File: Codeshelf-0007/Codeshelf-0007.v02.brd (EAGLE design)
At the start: 103.5 x 53 mm, 28 parts, among them J1 RJ45-8PTH, J2 RJ45-8PTH, U2 MC9S08QG-DT, U3 CAT9552, U4 RS485SOIC, U7 7SEGMENT-2DIGIT

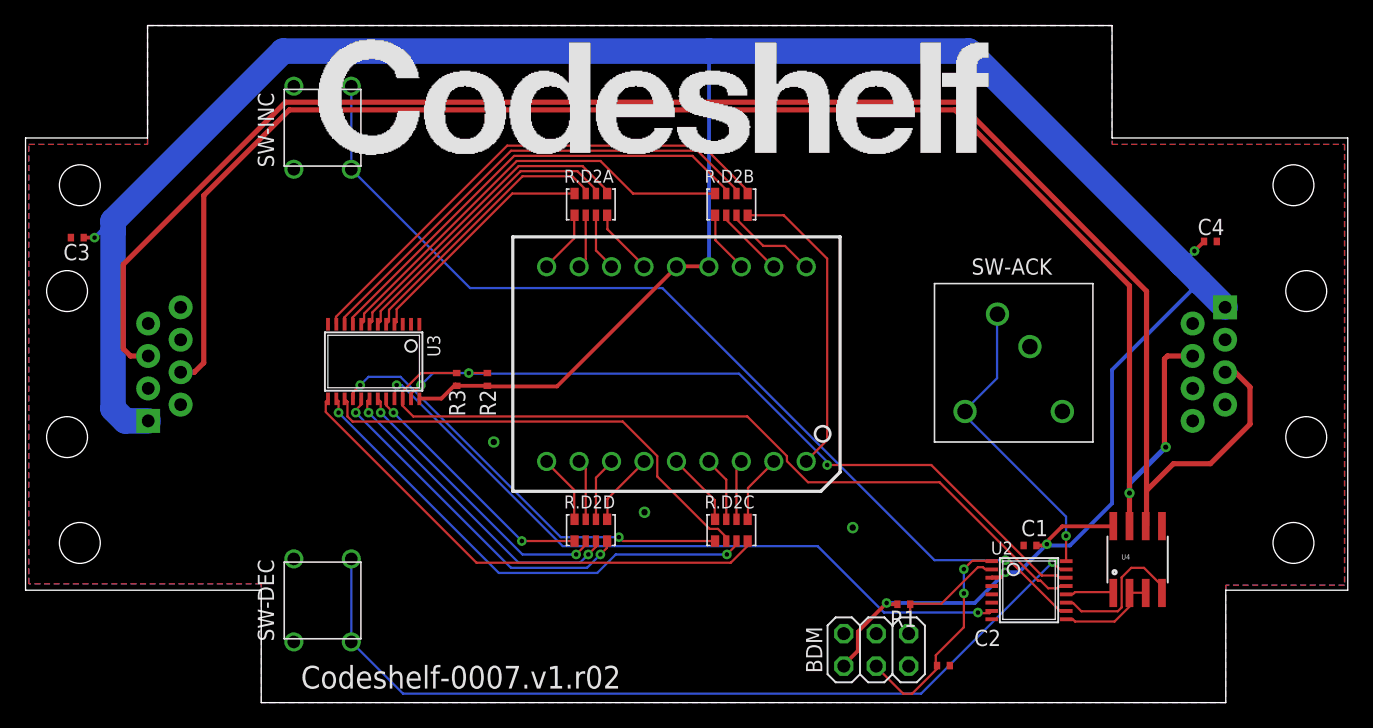
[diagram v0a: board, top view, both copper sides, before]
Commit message: Changes related to design review with Ravi and Charlie.
Mainly we need a new way to connect all of the boards where the cables
enter the back.
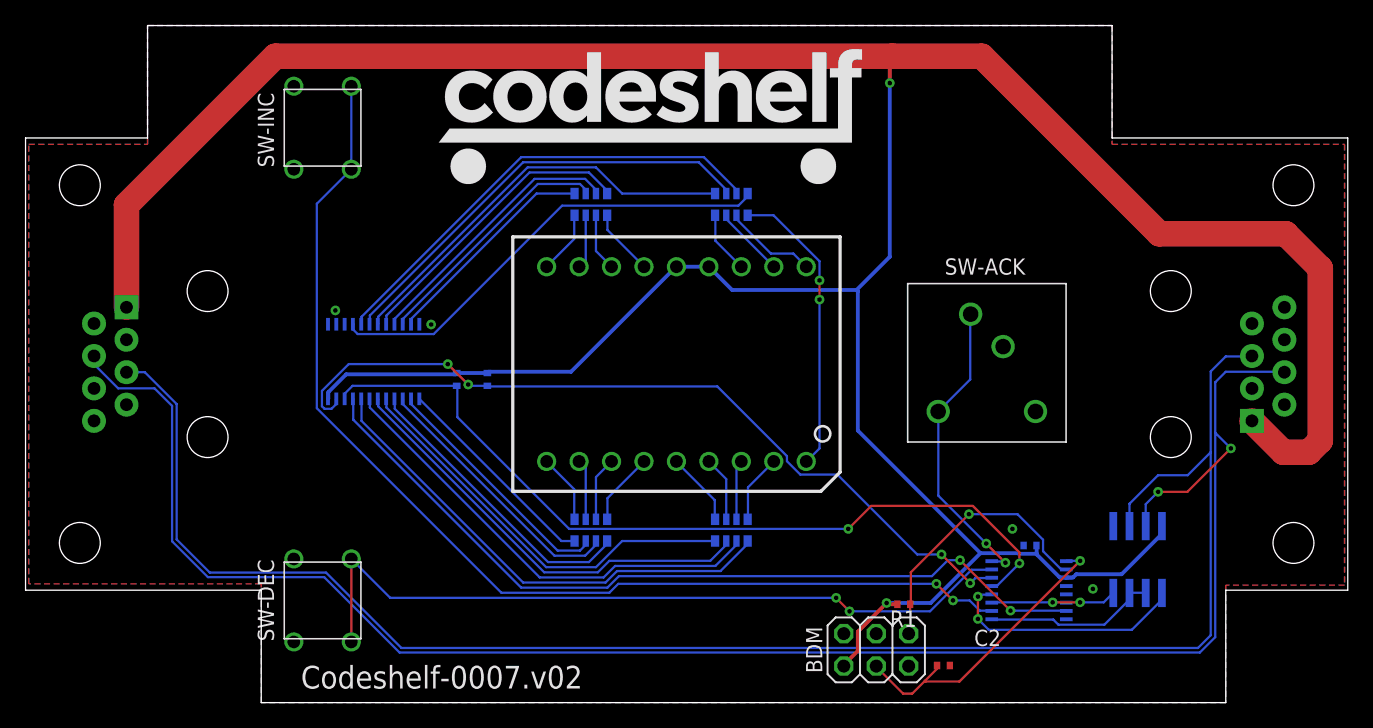
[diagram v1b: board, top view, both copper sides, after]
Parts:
- removed C3, C4: .1uF, GW-devices:C0402
- moved ACK.BUTTON.KEYCAP 115.3 mm to (95.7, 50.9)
- moved STANDOFF2 115.3 mm to (92.5, 47.5)
- moved STANDOFF3 115.3 mm to (91.5, 46.4)
- moved CASE 115.3 mm to (97.3, 52.6)
- moved STANDOFF1 115.3 mm to (94.1, 49.2)
- moved STANDOFF4 114.8 mm to (88.7, 47.7)
- moved LOGO 16.1 mm to (32.1, 40.6)
- moved J2 11.0 mm to (14.0, 26.5), turned to 270 degrees
- moved J1 10.6 mm to (89.4, 26.5), turned to 90 degrees
- moved SW-ACK 2.10 mm to (75.0, 26.6)
- flipped C1 to the bottom, turned to 0 degrees
- flipped R.D2A to the bottom
- flipped R.D2B to the bottom
- flipped R.D2C to the bottom
- flipped R.D2D to the bottom
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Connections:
- net A renamed RS485_P
- net B renamed RS485_N
- removed net N$39: R.D2C.3, U3.14
- removed net N$40: R.D2C.4, U3.13
- new net N$1: R.D2A.5, U3.11
- new net N$21: R.D2A.4, U7.18
- net +3V3: no longer C3.1, C4.1
- net GND: no longer C3.2, C4.2
- net N$10: now also R.D2B.6, U3.6; no longer R.D2B.1, U7.12
- net N$11: now also R.D2B.7, U3.5; no longer R.D2B.2, U7.11
- net N$12: now also R.D2B.8, U3.4; no longer R.D2B.3, U7.10
- net N$13: now also U7.4; no longer U7.1
- net N$14: now also U7.3; no longer U7.2
- net N$15: now also U7.2; no longer U7.3
- net N$16: now also U7.1; no longer U7.4
- net N$17: now also R.D2A.1, U7.15; no longer R.D2C.8, U7.5
- net N$18: now also R.D2A.2, U7.16; no longer R.D2C.7, U7.6
- net N$2: now also R.D2A.6, U3.10; no longer R.D2A.1, U7.18
- net N$20: now also R.D2A.3, U7.17; no longer R.D2C.6, U7.7
- net N$22: now also R.D2B.4, U7.12; no longer R.D2C.5, U7.8
- net N$24: now also R.D2B.3, U7.11; no longer R.D2B.4, U7.9
- net N$25: now also R.D2C.8, U7.8; no longer R.D2A.8, U3.4
- net N$26: now also R.D2C.7, U7.7; no longer R.D2A.7, U3.5
- net N$27: now also R.D2C.6, U7.6; no longer R.D2A.6, U3.6
- net N$28: now also R.D2C.5, U7.5; no longer R.D2A.5, U3.7
- net N$29: now also R.D2B.1, U7.9; no longer R.D2B.8, U3.8
- net N$3: now also R.D2A.7, U3.9; no longer R.D2A.2, U7.17
- net N$30: now also R.D2B.2, U7.10; no longer R.D2B.7, U3.9
- net N$31: now also R.D2D.4, U3.13; no longer R.D2B.6, U3.10
- net N$32: now also R.D2D.3, U3.14; no longer R.D2B.5, U3.11
- net N$33: now also R.D2D.2, U3.15; no longer R.D2D.1, U3.20
- net N$34: now also R.D2D.1, U3.16; no longer R.D2D.2, U3.19
- net N$35: now also R.D2C.4, U3.17; no longer R.D2D.3, U3.18
- net N$36: now also R.D2C.3, U3.18; no longer R.D2D.4, U3.17
- net N$37: now also R.D2C.2, U3.19; no longer R.D2C.1, U3.16
- net N$38: now also R.D2C.1, U3.20; no longer R.D2C.2, U3.15
- net N$4: now also R.D2A.8, U3.8; no longer R.D2A.3, U7.16
- net N$5: now also R.D2B.5, U3.7; no longer R.D2A.4, U7.15
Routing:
- net N$40: track 40.0 -> 0.00 mm
- net N$39: track 38.7 -> 0.00 mm, vias 2 -> 0
- net +3V3: track 224.1 -> 258.1 mm, vias 5 -> 2
- net N$11: track 5.61 -> 36.5 mm
- net N$10: track 4.91 -> 34.8 mm
- net N$30: track 36.4 -> 7.31 mm
- net N$12: track 7.33 -> 36.2 mm
- net N$5: track 5.28 -> 32.7 mm
- net N$31: track 38.2 -> 16.8 mm
- net N$32: track 40.1 -> 19.3 mm
- net N$28: track 25.2 -> 5.80 mm
- net N$4: track 4.56 -> 23.4 mm
- net N$24: track 24.2 -> 5.57 mm
- net N$27: track 23.4 -> 5.09 mm
- net N$1: track 0.00 -> 17.3 mm
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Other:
- board text added: "Codeshelf-0007.v02"
- board text removed: "Codeshelf-0007.v1.r02"

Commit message: Position controller bus rewiring
The position controller's RS495 bus rewired to support double 3.3V/GND
and to be off of the same pins as the scanner.  (Matches the change
with the CHE controller.)
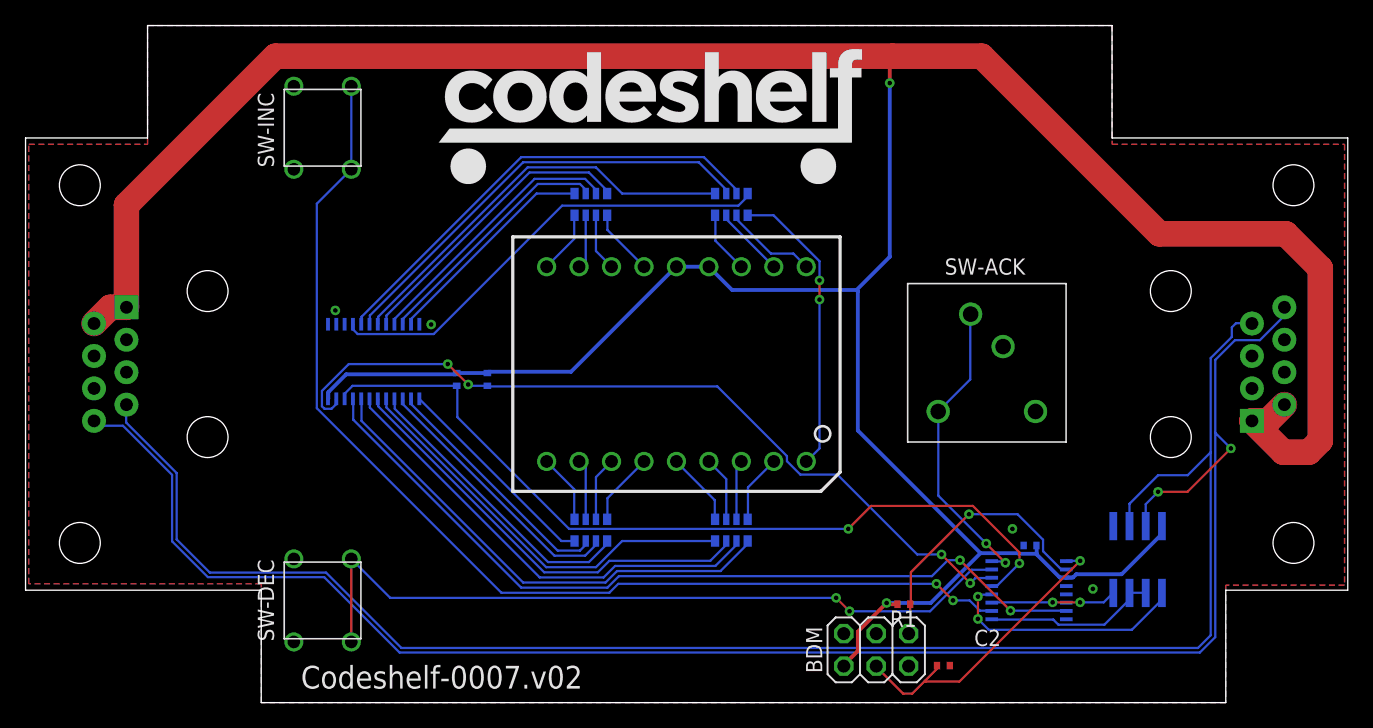
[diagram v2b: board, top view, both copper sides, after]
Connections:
- net +3V3: now also J1.2, J2.2
- net GND: now also J1.3, J1.6, J2.3, J2.6; no longer J1.8, J2.8
- net RS485_N: now also J1.8, J2.8; no longer J1.4, J2.4
- net RS485_P: now also J1.7, J2.7; no longer J1.5, J2.5
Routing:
- net +3V3: track 258.1 -> 264.2 mm
- net RS485_N: track 142.1 -> 140.0 mm
- net RS485_P: track 134.6 -> 133.4 mm
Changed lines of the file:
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@@
 <contactref element="SW-DEC" pad="P$3"/>
 <contactref element="SW-ACK" pad="P$3"/>
-<contactref element="J1" pad="8"/>
-<contactref element="J2" pad="8"/>
 <polygon width="0.4064" layer="1">
 <vertex x="0" y="9.3"/>
@@
 <via x="77" y="13.6" extent="1-16" drill="0.3556"/>
 <via x="83.3" y="8.9" extent="1-16" drill="0.3556"/>
+<contactref element="J2" pad="6"/>
+<contactref element="J2" pad="3"/>
+<contactref element="J1" pad="3"/>
+<contactref element="J1" pad="6"/>
 </signal>
 <signal name="+3V3" class="1">
@@
 <wire x1="64.9" y1="32.2" x2="64.8" y2="32.3" width="0.3" layer="16"/>
 <via x="67.15" y="7.8" extent="1-16" drill="0.3556"/>
+<contactref element="J2" pad="2"/>
+<contactref element="J1" pad="2"/>
+<wire x1="7.65" y1="30.945" x2="6.38" y2="30.945" width="2" layer="1"/>
+<wire x1="6.38" y1="30.945" x2="5.11" y2="29.675" width="2" layer="1"/>
+<wire x1="95.75" y1="22.055" x2="97.02" y2="22.055" width="2" layer="1"/>
+<wire x1="97.02" y1="22.055" x2="98.29" y2="23.325" width="2" layer="1"/>
 </signal>
 <signal name="SLC">
@@
 </signal>
 <signal name="RS485_N">
-<contactref element="J2" pad="4"/>
-<contactref element="J1" pad="4"/>
 <contactref element="U4" pad="7"/>
-<wire x1="5.11" y1="27.135" x2="5.11" y2="26.49" width="0.1778" layer="16"/>
-<wire x1="5.11" y1="26.49" x2="7" y2="24.6" width="0.1778" layer="16"/>
-<wire x1="7" y1="24.6" x2="9.84855" y2="24.6" width="0.1778" layer="16"/>
-<wire x1="9.84855" y1="24.6" x2="11.2222" y2="23.22635" width="0.1778" layer="16"/>
-<wire x1="11.2222" y1="23.22635" x2="11.2222" y2="12.62635" width="0.1778" layer="16"/>
 <wire x1="11.2222" y1="12.62635" x2="14.02635" y2="9.8222" width="0.1778" layer="16"/>
 <wire x1="14.02635" y1="9.8222" x2="23.12635" y2="9.8222" width="0.1778" layer="16"/>
@@
 <wire x1="91.67365" y1="3.9222" x2="92.8778" y2="5.12635" width="0.1778" layer="16"/>
 <wire x1="92.8778" y1="5.12635" x2="92.8778" y2="21.1222" width="0.1778" layer="16"/>
-<wire x1="92.8778" y1="21.1222" x2="92.8778" y2="25.0778" width="0.1778" layer="16"/>
-<wire x1="92.8778" y1="25.0778" x2="93.7" y2="25.9" width="0.1778" layer="16"/>
-<wire x1="93.7" y1="25.9" x2="98.255" y2="25.9" width="0.1778" layer="16"/>
-<wire x1="98.255" y1="25.9" x2="98.29" y2="25.865" width="0.1778" layer="16"/>
 <wire x1="87.435" y1="13.8162" x2="87.435" y2="15.535" width="0.1778" layer="16"/>
 <wire x1="87.435" y1="15.535" x2="88.4" y2="16.5" width="0.1778" layer="16"/>
@@
 <via x="94.1" y="19.9" extent="1-16" drill="0.3556"/>
 <wire x1="94.1" y1="19.9" x2="92.8778" y2="21.1222" width="0.1778" layer="16"/>
+<wire x1="92.8778" y1="21.1222" x2="92.8778" y2="26.82635" width="0.1778" layer="16"/>
+<contactref element="J2" pad="8"/>
+<contactref element="J1" pad="8"/>
+<wire x1="11.2222" y1="12.62635" x2="11.2222" y2="17.82635" width="0.1778" layer="16"/>
+<wire x1="11.2222" y1="17.82635" x2="7.374275" y2="21.674275" width="0.1778" layer="16"/>
+<wire x1="7.374275" y1="21.674275" x2="5.490725" y2="21.674275" width="0.1778" layer="16"/>
+<wire x1="5.490725" y1="21.674275" x2="5.11" y2="22.055" width="0.1778" layer="16"/>
+<wire x1="92.8778" y1="26.82635" x2="94.425725" y2="28.374275" width="0.1778" layer="16"/>
+<wire x1="94.425725" y1="28.374275" x2="96.374275" y2="28.374275" width="0.1778" layer="16"/>
+<wire x1="96.374275" y1="28.374275" x2="98.3" y2="30.3" width="0.1778" layer="16"/>
+<wire x1="98.3" y1="30.3" x2="98.3" y2="30.935" width="0.1778" layer="16"/>
+<wire x1="98.3" y1="30.935" x2="98.29" y2="30.945" width="0.1778" layer="16"/>
 </signal>
 <signal name="N$6">
@@
 </signal>
 <signal name="RS485_P">
-<contactref element="J2" pad="5"/>
 <contactref element="U4" pad="6"/>
-<contactref element="J1" pad="5"/>
-<wire x1="7.65" y1="25.865" x2="9.08645" y2="25.865" width="0.1778" layer="16"/>
-<wire x1="9.08645" y1="25.865" x2="11.5778" y2="23.37365" width="0.1778" layer="16"/>
-<wire x1="11.5778" y1="23.37365" x2="11.5778" y2="12.77365" width="0.1778" layer="16"/>
 <wire x1="11.5778" y1="12.77365" x2="14.17365" y2="10.1778" width="0.1778" layer="16"/>
 <wire x1="14.17365" y1="10.1778" x2="23.27365" y2="10.1778" width="0.1778" layer="16"/>
@@
 <wire x1="91.52635" y1="4.2778" x2="92.5222" y2="5.27365" width="0.1778" layer="16"/>
 <wire x1="92.5222" y1="5.27365" x2="92.5222" y2="19.6" width="0.1778" layer="16"/>
-<wire x1="92.5222" y1="19.6" x2="92.5222" y2="25.9222" width="0.1778" layer="16"/>
-<wire x1="92.5222" y1="25.9222" x2="93.7" y2="27.1" width="0.1778" layer="16"/>
-<wire x1="93.7" y1="27.1" x2="95.715" y2="27.1" width="0.1778" layer="16"/>
-<wire x1="95.715" y1="27.1" x2="95.75" y2="27.135" width="0.1778" layer="16"/>
+<wire x1="92.5222" y1="19.6" x2="92.5222" y2="26.97365" width="0.1778" layer="16"/>
 <wire x1="86.165" y1="13.8162" x2="86.165" y2="15.565" width="0.1778" layer="16"/>
 <wire x1="86.165" y1="15.565" x2="88.4" y2="17.8" width="0.1778" layer="16"/>
 <wire x1="88.4" y1="17.8" x2="90.7222" y2="17.8" width="0.1778" layer="16"/>
 <wire x1="90.7222" y1="17.8" x2="92.5222" y2="19.6" width="0.1778" layer="16"/>
+<contactref element="J2" pad="7"/>
+<contactref element="J1" pad="7"/>
+<wire x1="11.5778" y1="12.77365" x2="11.5778" y2="17.97365" width="0.1778" layer="16"/>
+<wire x1="11.5778" y1="17.97365" x2="7.625725" y2="21.925725" width="0.1778" layer="16"/>
+<wire x1="7.625725" y1="21.925725" x2="7.625725" y2="23.300725" width="0.1778" layer="16"/>
+<wire x1="7.625725" y1="23.300725" x2="7.65" y2="23.325" width="0.1778" layer="16"/>
+<wire x1="92.5222" y1="26.97365" x2="94.174275" y2="28.625725" width="0.1778" layer="16"/>
+<wire x1="94.174275" y1="28.625725" x2="94.174275" y2="29.374275" width="0.1778" layer="16"/>
+<wire x1="94.174275" y1="29.374275" x2="94.5" y2="29.7" width="0.1778" layer="16"/>
+<wire x1="94.5" y1="29.7" x2="95.725" y2="29.7" width="0.1778" layer="16"/>
+<wire x1="95.725" y1="29.7" x2="95.75" y2="29.675" width="0.1778" layer="16"/>
 </signal>
 <signal name="N$1">

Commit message: Changes reviewed with Charlie
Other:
- board text added: "CS0007.2013.11.24.n1"
- board text removed: "Codeshelf-0007.v02"
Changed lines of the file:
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@@
 <wire x1="84.8" y1="53" x2="84.8" y2="44.2" width="0" layer="20"/>
 <wire x1="84.8" y1="44.2" x2="103.25" y2="44.2" width="0" layer="20"/>
-<text x="21.3" y="1.1" size="1.778" layer="21">Codeshelf-0007.v02</text>
+<text x="23.3" y="1.1" size="1.778" layer="21">CS0007.2013.11.24.n1</text>
 <hole x="4" y="12.5" drill="3.2"/>
 <hole x="4" y="40.5" drill="3.2"/>
@@
 <element name="LOGO" library="GW-devices" package="CODESHELF-LOGO" value="CODESHELF-LOGO" x="32.1" y="40.6"/>
 <element name="BDM" library="GW-devices" package="HEADER-3X2" value="HEADER-3X2" x="63.8" y="5.4" smashed="yes" rot="R180">
-<attribute name="NAME" x="60.845" y="5.95" size="1.27" layer="25" ratio="10" rot="R270"/>
+<attribute name="NAME" x="60.645" y="8.05" size="1.27" layer="25" ratio="10" rot="R270"/>
 </element>
 <element name="R1" library="GW-devices" package="RF-R0402" value="3.3K" x="68.5" y="7.7" smashed="yes" rot="R180">
@@
 </element>
 <element name="SW-DEC" library="GW-devices" package="SWITCH-TACTILE-FSM" value="SWITCH-TACTILE-FSM" x="23" y="8" smashed="yes" rot="R270">
-<attribute name="NAME" x="19.2" y="4.8" size="1.27" layer="25" rot="R90"/>
+<attribute name="NAME" x="26.8" y="13.6" size="1.27" layer="25" rot="R180"/>
 <attribute name="MFGN" value="TE Connectivity" x="23" y="8" size="1.778" layer="27" rot="R270" display="off"/>
 <attribute name="MFGP" value="FSM16JH" x="23" y="8" size="1.778" layer="27" rot="R270" display="off"/>
@@
 </element>
 <element name="SW-INC" library="GW-devices" package="SWITCH-TACTILE-FSM" value="SWITCH-TACTILE-FSM" x="23" y="45" smashed="yes" rot="R270">
-<attribute name="NAME" x="19.2" y="41.9" size="1.27" layer="25" rot="R90"/>
+<attribute name="NAME" x="19.9" y="39.4" size="1.27" layer="25"/>
 <attribute name="MFGN" value="TE Connectivity" x="23" y="45" size="1.778" layer="27" rot="R270" display="off"/>
 <attribute name="MFGP" value="FSM16JH" x="23" y="45" size="1.778" layer="27" rot="R270" display="off"/>

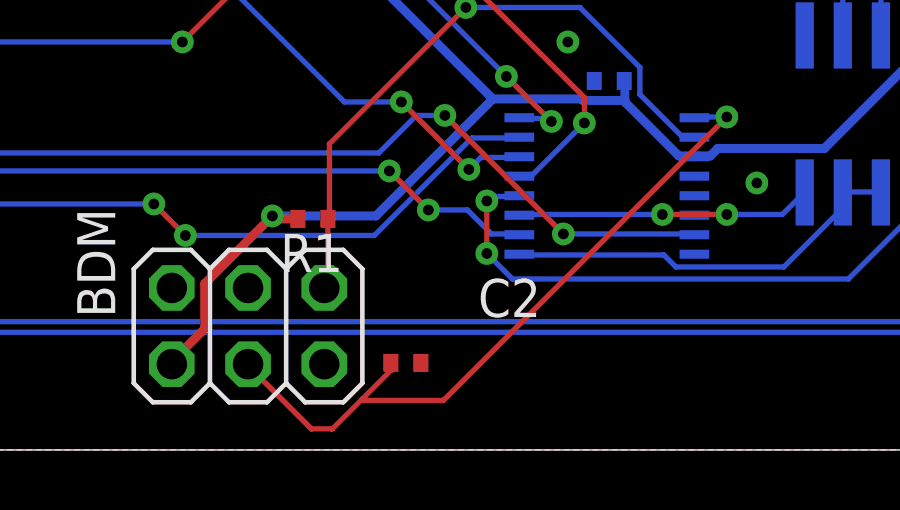
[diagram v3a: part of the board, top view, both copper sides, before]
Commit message: BOM review before first articles of 0005, 0007, 0008, 0012
Reviewed BOM with Charlie
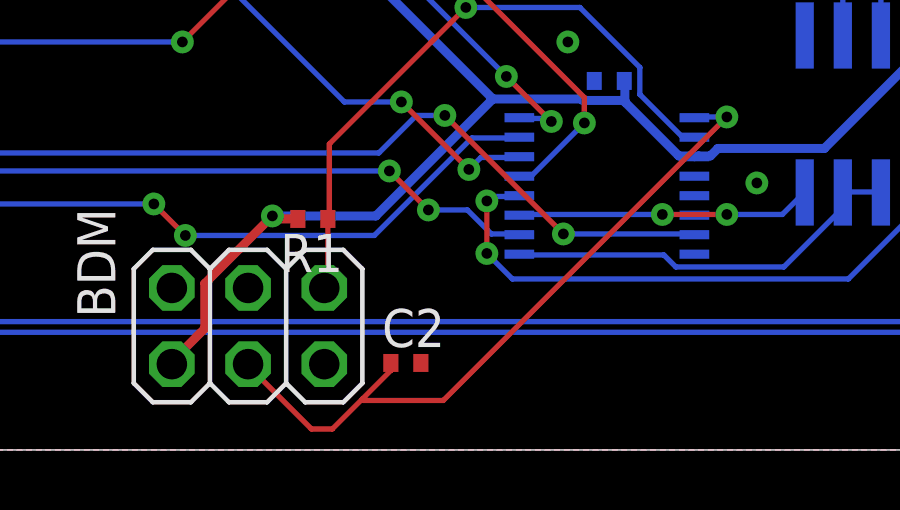
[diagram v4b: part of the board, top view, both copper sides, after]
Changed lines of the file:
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@@
 <attribute name="NAME" x="79.78" y="10.3" size="1.27" layer="26" rot="MR0"/>
 <attribute name="MFGN" value="Murata" x="78.38" y="12.3" size="1.778" layer="28" rot="MR0" display="off"/>
-<attribute name="MFGP" value="GRM033R61A104KE15D" x="78.38" y="12.3" size="1.778" layer="28" rot="MR0" display="off"/>
+<attribute name="MFGP" value="
+GRM155R61C104KA88D" x="78.38" y="12.3" size="1.778" layer="28" rot="MR0" display="off"/>
 <attribute name="PRICE" value="0.02" x="78.38" y="12.3" size="1.778" layer="28" rot="MR0" display="off"/>
 </element>
@@
 </element>
 <element name="C2" library="GW-devices" package="C0402" value=".1uF" x="71.6" y="2.9" smashed="yes" rot="R180">
-<attribute name="NAME" x="76.1" y="5.7" size="1.27" layer="25" rot="R180"/>
+<attribute name="NAME" x="72.9" y="4.7" size="1.27" layer="25" rot="R180"/>
 <attribute name="MFGN" value="Murata" x="71.6" y="2.9" size="1.778" layer="27" rot="R180" display="off"/>
-<attribute name="MFGP" value="GRM033R61A104KE15D" x="71.6" y="2.9" size="1.778" layer="27" rot="R180" display="off"/>
+<attribute name="MFGP" value="
+GRM155R61C104KA88D" x="71.6" y="2.9" size="1.778" layer="27" rot="R180" display="off"/>
 <attribute name="PRICE" value="0.02" x="71.6" y="2.9" size="1.778" layer="27" rot="R180" display="off"/>
 </element>
@@
 <attribute name="NAME" x="35.3" y="26.1" size="1.27" layer="26" rot="MR90"/>
 <attribute name="MFGN" value="Panasonic" x="35.9" y="25.3" size="1.778" layer="28" rot="MR90" display="off"/>
-<attribute name="MFGP" value="ERJ-2GEJ332X" x="35.9" y="25.3" size="1.778" layer="28" rot="MR90" display="off"/>
+<attribute name="MFGP" value="ERJ-2GEJ103X" x="35.9" y="25.3" size="1.778" layer="28" rot="MR90" display="off"/>
 <attribute name="PRICE" value="0.02" x="35.9" y="25.3" size="1.778" layer="28" rot="MR90" display="off"/>
 </element>
@@
 <attribute name="NAME" x="32.9" y="26.1" size="1.27" layer="26" rot="MR90"/>
 <attribute name="MFGN" value="Panasonic" x="33.5" y="25.3" size="1.778" layer="28" rot="MR90" display="off"/>
-<attribute name="MFGP" value="ERJ-2GEJ332X" x="33.5" y="25.3" size="1.778" layer="28" rot="MR90" display="off"/>
+<attribute name="MFGP" value="ERJ-2GEJ103X" x="33.5" y="25.3" size="1.778" layer="28" rot="MR90" display="off"/>
 <attribute name="PRICE" value="0.02" x="33.5" y="25.3" size="1.778" layer="28" rot="MR90" display="off"/>
 </element>
